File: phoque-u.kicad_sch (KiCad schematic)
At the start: 66 parts, among them J1 18…56 V, J2 On / Off, J3 3.3…24 V, Q1 SiR120DP, Q2 SiR120DP, Q3 SiR120DP, Q4 SiR120DP, SW1 Remote, SW2 Voltage select, T1 320 µ, T2 180 µ, U1 LT4320, U2 i7A4W033A033V

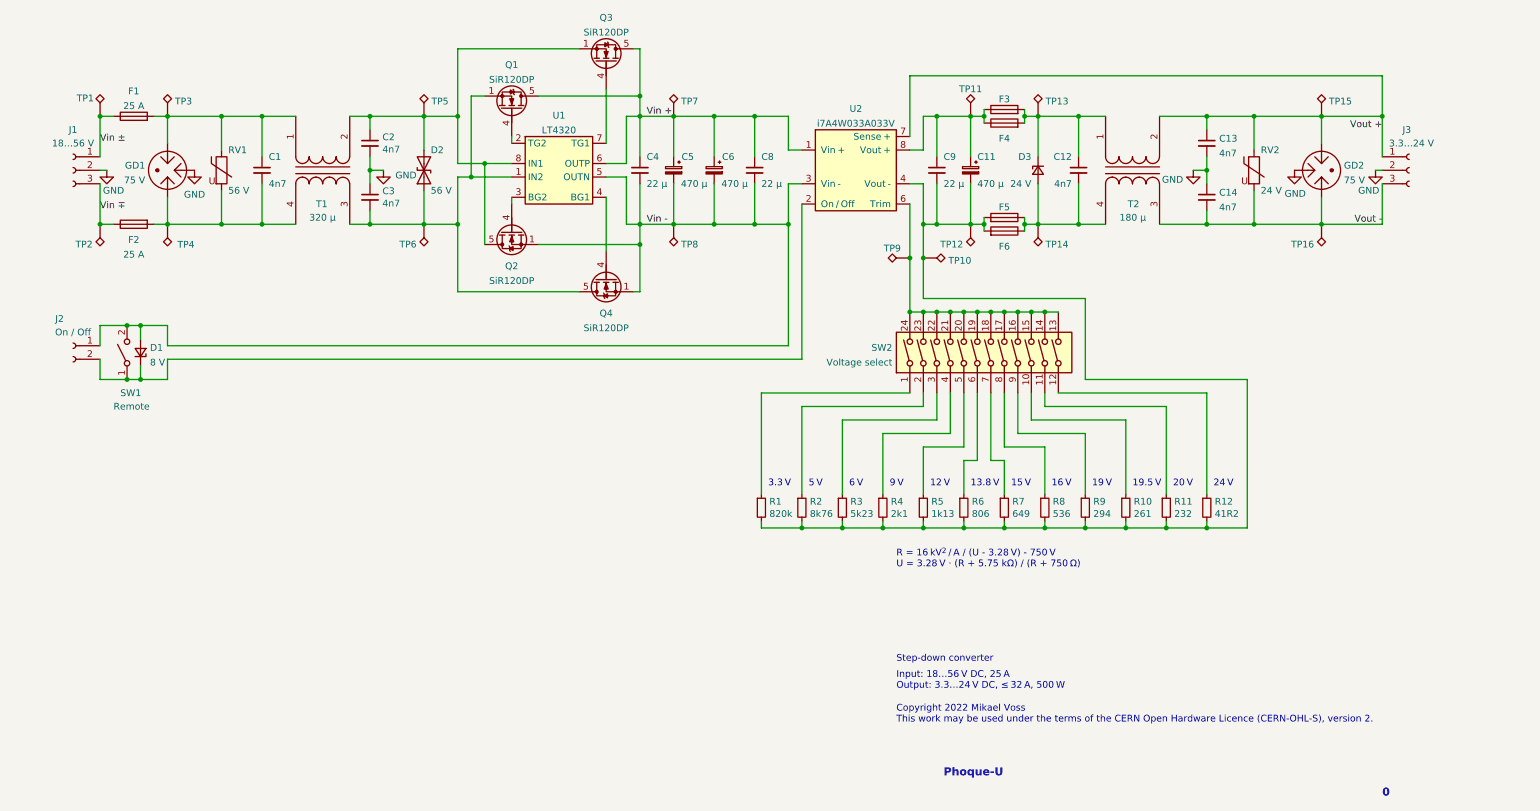
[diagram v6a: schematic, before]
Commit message: Remove test points
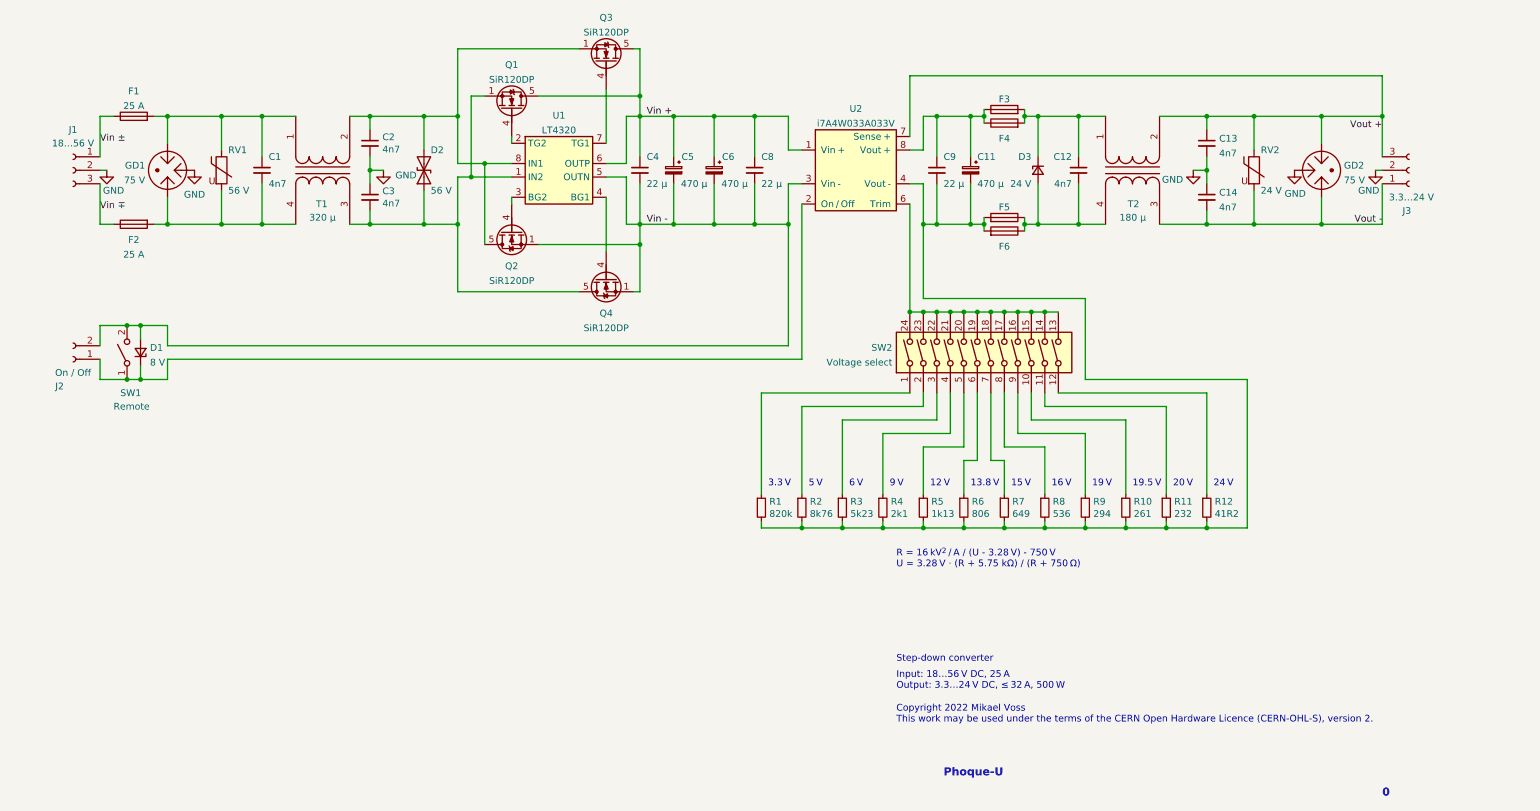
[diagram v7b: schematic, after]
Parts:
- removed TP1, TP10, TP11, TP12, TP13, TP14, TP15, TP16, TP2, TP3, TP4, TP5, TP6, TP7, TP8, TP9: test, TestPoint:TestPoint_Pad_D1.5mm, symbol Connector:TestPoint_Alt
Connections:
- net Vin -: now also J2.2 (Pin_2); no longer J2.1 (Pin_1)
- net Vout +: now also J3.3 (Pin_3); no longer J3.1 (Pin_1)
- net Vout -: now also J3.1 (Pin_1); no longer J3.3 (Pin_3)
- net at D1.1 (K), SW1.1 (A), U2.2 (On / Off): now also J2.1 (Pin_1); no longer J2.2 (Pin_2)
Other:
- moved on the sheet: J2

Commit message: Add initial PCB layout
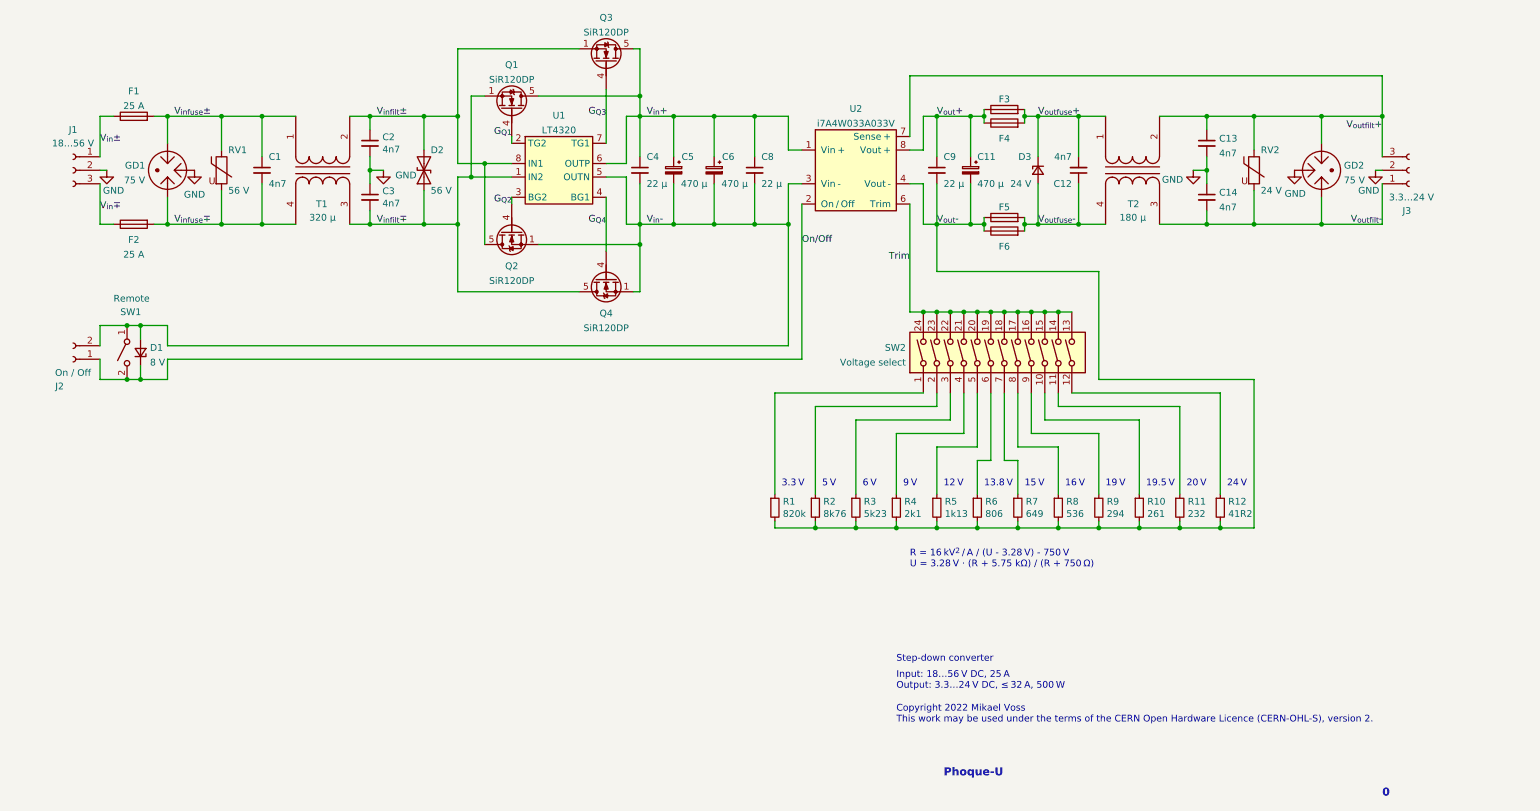
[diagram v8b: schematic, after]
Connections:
- net V_{infuse}±: now reaches C1.1, F1.2, GD1.1, RV1.1, T1.1 (AA)
- net V_{infilt}±: now reaches C2.1, D2.2 (A2), Q2.5 (D), Q3.1 (S), Q3.2 (S), Q3.3 (S), T1.2 (AB), U1.8 (IN1)
- net V_{infilt}∓: now reaches C3.2, D2.1 (A1), Q1.1 (S), Q1.2 (S), Q1.3 (S), Q4.5 (D), T1.3 (SA), U1.1 (IN2)
- net V_{infuse}∓: now reaches C1.2, F2.2, GD1.3, RV1.2, T1.4 (SB)
- net V_{outfuse}+: now reaches D3.1 (K), F3.2, F4.2, T2.1 (AA)
- net V_{outfuse}+: now also C12.2; no longer C12.1
- net V_{out}+: now reaches C11.1, C9.1, F3.1, F4.1, U2.8 (Vout +)
- net V_{out}-: now reaches C11.2, C9.2, R1.2, R10.2, R11.2, R12.2, R2.2, R3.2, R4.2, R5.2, R6.2, R7.2, R8.2, R9.2, U2.4 (Vout -)
- net V_{out}-: now also F5.1, F6.1; no longer F5.2, F6.2
- net On/Off: now reaches D1.1 (K), J2.1 (Pin_1), U2.2 (On / Off)
- net On/Off: now also SW1.2 (B); no longer SW1.1 (A)
- net Trim: now reaches SW2.13, SW2.14, SW2.15, SW2.16, SW2.17, SW2.18, SW2.19, SW2.20, SW2.21, SW2.22, SW2.23, SW2.24, U2.6 (Trim)
- net G_{Q1}: now reaches Q1.4 (G), U1.2 (TG2)
- net G_{Q3}: now reaches Q3.4 (G), U1.7 (TG1)
- net G_{Q4}: now reaches Q4.4 (G), U1.4 (BG1)
- net G_{Q2}: now reaches Q2.4 (G), U1.3 (BG2)
- net Vin + renamed V_{in}+
- net Vin - renamed V_{in}-
- net V_{in}-: now also SW1.1 (A); no longer SW1.2 (B)
- net Vin ± renamed V_{in}±
- net Vin ∓ renamed V_{in}∓
- net Vout + renamed V_{outfilt}+
- net Vout - renamed V_{outfilt}-
- new net V_{outfuse}-: C12.1, D3.2 (A), F5.2, F6.2, T2.4 (SB)
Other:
- moved on the sheet: C12, F5, F6, R1, R10, R11, R12, R2, R3, R4, R5, R6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
